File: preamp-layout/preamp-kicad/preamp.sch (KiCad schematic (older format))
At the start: 12 parts, among them P1 Conn_WallPlug, SW1 Rotary_Encoder_Switch, SW10 SW_Push_Open, SW11 SW_Push_Open, SW2 Rotary_Encoder_Switch, SW3 SW_SPST, SW4 SW_Push_Open, SW5 SW_Push_Open, SW6 SW_Push_Open, SW7 SW_Push_Open, SW8 SW_Push_Open, SW9 SW_Push_Open

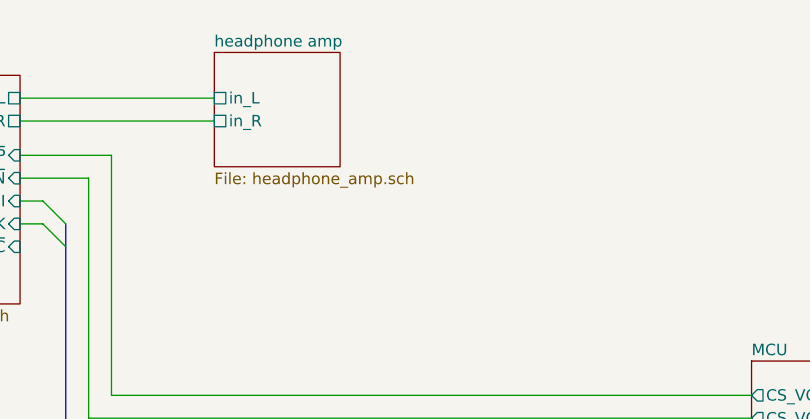
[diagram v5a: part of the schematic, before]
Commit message: Headphone Amp Crossfeed Implementation - using the CMOY modified Linkwitz High Z crossfeed design as a basis.
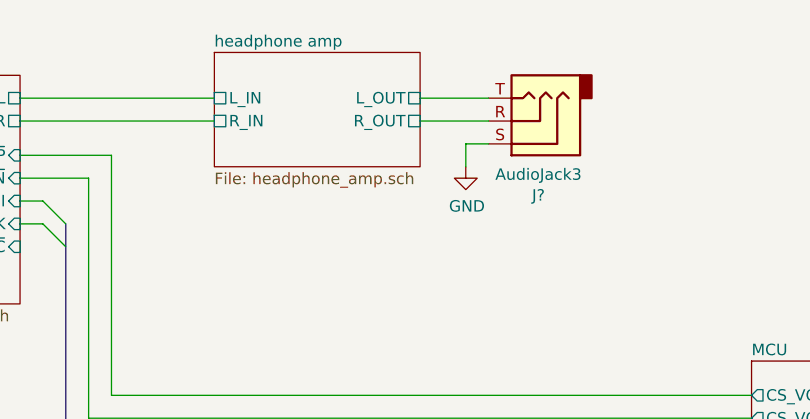
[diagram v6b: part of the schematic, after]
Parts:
- added J?: AudioJack3, symbol Connector:AudioJack3
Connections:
- net GND: now also J?.S
- new net headphone amp/L_OUT: J?.T
- new net headphone amp/R_OUT: J?.R
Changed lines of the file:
@@
 EESchema Schematic File Version 4
+LIBS:preamp-cache
 EELAYER 30 0
 EELAYER END
 $Descr A4 11693 8268
 encoding utf-8
-Sheet 1 12
+Sheet 1 13
 Title "Preamp"
-Date "2020-01-23"
+Date "2020-02-25"
 Rev "A00"
 Comp ""
@@
 F2 "AC+" U L 3200 7100 50
 F3 "AC-" U L 3200 7200 50
-$EndSheet
-$Sheet
-S 5850 950  550  500
-U 5E4A803E
-F0 "headphone amp" 50
-F1 "headphone_amp.sch" 50
-F2 "in_R" U L 5850 1250 50
-F3 "in_L" U L 5850 1150 50
 $EndSheet
 $Sheet
@@
 $EndSheet
 $Sheet
-S 1400 4350 550  550
-U 5E1A0CE1
-F0 "Balanced daughter IO pcb" 50
-F1 "IO_BALANCED_DAUGHTER.sch" 50
-F2 "OUT_R" U R 1950 4800 50
-F3 "OUT_L" U R 1950 4700 50
-F4 "IN_L" U R 1950 4450 50
-F5 "IN_R" U R 1950 4550 50
-$EndSheet
-$Sheet
 S 850  900  750  2450
 U 5E607732
@@
 F15 "A_OUT_2_L" U R 1600 3100 50
 $EndSheet
-Text Label 2200 4450 0    50   ~ 0
-BAL_IN_L
-Text Label 2200 4550 0    50   ~ 0
-BAL_IN_R
-Text Label 2200 4700 0    50   ~ 0
-BAL_OUT_L
-Text Label 2200 4800 0    50   ~ 0
-BAL_OUT_R
-Text Label 1950 2350 3    50   ~ 0
-BAL_IN_L
-Text Label 1850 2350 3    50   ~ 0
-BAL_IN_R
-Text Label 1950 3400 3    50   ~ 0
-BAL_OUT_L
-Text Label 1850 3400 3    50   ~ 0
-BAL_OUT_R
 $Comp
 L Device:Rotary_Encoder_Switch SW?
@@
 	2650 6150 3050 6150
 Wire Wire Line
-	1950 4450 2200 4450
-Wire Wire Line
-	1950 4550 2200 4550
-Wire Wire Line
-	1950 4700 2200 4700
-Wire Wire Line
-	1950 4800 2200 4800
-Wire Wire Line
 	1600 2850 2150 2850
 Wire Wire Line
 	1600 2950 2150 2950
 Wire Wire Line
-	1600 3100 1950 3100
-Wire Wire Line
-	1600 3200 1850 3200
-Wire Wire Line
-	1600 2150 1850 2150
-Wire Wire Line
-	1600 2050 1950 2050
-Wire Wire Line
 	1600 1000 2150 1000
 Wire Wire Line
@@
 Wire Wire Line
 	1600 1850 2150 1850
-Wire Wire Line
-	1950 2350 1950 2050
-Connection ~ 1950 2050
-Wire Wire Line
-	1950 2050 2150 2050
-Wire Wire Line
-	1850 2350 1850 2150
-Connection ~ 1850 2150
-Wire Wire Line
-	1850 2150 2150 2150
-Wire Wire Line
-	1950 3400 1950 3100
-Connection ~ 1950 3100
-Wire Wire Line
-	1950 3100 2150 3100
-Wire Wire Line
-	1850 3400 1850 3200
-Connection ~ 1850 3200
-Wire Wire Line
-	1850 3200 2150 3200
 Wire Wire Line
 	10450 2400 10750 2400
@@
 Connection ~ 10750 2900
 Connection ~ 10750 3450
-Wire Bus Line
-	5200 1700 5200 3300
-Wire Bus Line
-	8000 3300 8000 3500
-Wire Bus Line
-	3600 2850 3600 3300
-Wire Bus Line
-	6650 3300 6650 4050
 $Sheet
 S 4250 1050 750  1000
@@
 F12 "CLK" I R 5000 1700 50
 $EndSheet
+$Comp
+L Connector:AudioJack3 J?
+U 1 1 5F4B3F32
+P 7250 1250
+AR Path="/5E4A803E/5F4B3F32" Ref="J?"  Part="1"
+AR Path="/5F4B3F32" Ref="J?"  Part="1"
+F 0 "J?" H 7232 1575 50  0000 C CNN
+F 1 "AudioJack3" H 7232 1484 50  0000 C CNN
+F 2 "" H 7250 1250 50  0001 C CNN
+F 3 "~" H 7250 1250 50  0001 C CNN
+	1    7250 1250
+	-1   0    0    1
+$EndComp
+$Comp
+L power:GND #PWR?
+U 1 1 5F4B3F39
+P 6950 1450
+AR Path="/6009D432/5F4B3F39" Ref="#PWR?"  Part="1"
+AR Path="/5E4A803E/5F4B3F39" Ref="#PWR?"  Part="1"
+AR Path="/5F4B3F39" Ref="#PWR?"  Part="1"
+F 0 "#PWR?" H 6950 1200 50  0001 C CNN
+F 1 "GND" H 6955 1277 50  0000 C CNN
+F 2 "" H 6950 1450 50  0001 C CNN
+F 3 "" H 6950 1450 50  0001 C CNN
+	1    6950 1450
+	1    0    0    -1
+$EndComp
+Wire Wire Line
+	6950 1450 6950 1350
+Wire Wire Line
+	6950 1350 7050 1350
+Wire Wire Line
+	6750 1150 7050 1150
+Wire Wire Line
+	6750 1250 7050 1250
+$Sheet
+S 5850 950  900  500
+U 5E4A803E
+F0 "headphone amp" 50
+F1 "headphone_amp.sch" 50
+F2 "R_IN" U L 5850 1250 50
+F3 "L_IN" U L 5850 1150 50
+F4 "L_OUT" U R 6750 1150 50
+F5 "R_OUT" U R 6750 1250 50
+$EndSheet
+Wire Wire Line
+	1850 3200 2150 3200
+Wire Wire Line
+	1600 3200 1850 3200
+Connection ~ 1850 3200
+Wire Wire Line
+	1850 3400 1850 3200
+Wire Wire Line
+	1950 3100 2150 3100
+Wire Wire Line
+	1600 3100 1950 3100
+Connection ~ 1950 3100
+Wire Wire Line
+	1950 3400 1950 3100
+Text Label 1850 3400 3    50   ~ 0
+BAL_OUT_R
+Text Label 1950 3400 3    50   ~ 0
+BAL_OUT_L
+Wire Wire Line
+	1850 2150 2150 2150
+Wire Wire Line
+	1600 2150 1850 2150
+Connection ~ 1850 2150
+Wire Wire Line
+	1850 2350 1850 2150
+Wire Wire Line
+	1950 2050 2150 2050
+Wire Wire Line
+	1600 2050 1950 2050
+Connection ~ 1950 2050
+Wire Wire Line
+	1950 2350 1950 2050
+Text Label 1850 2350 3    50   ~ 0
+BAL_IN_R
+Text Label 1950 2350 3    50   ~ 0
+BAL_IN_L
+Wire Bus Line
+	5200 1700 5200 3300
+Wire Bus Line
+	6650 3300 6650 4050
+Wire Bus Line
+	8000 3300 8000 3500
+Wire Bus Line
+	3600 2850 3600 3300
+Wire Wire Line
+	1950 4800 2200 4800
+Wire Wire Line
+	1950 4700 2200 4700
+Wire Wire Line
+	1950 4550 2200 4550
+Wire Wire Line
+	1950 4450 2200 4450
+Text Label 2200 4800 0    50   ~ 0
+BAL_OUT_R
+Text Label 2200 4700 0    50   ~ 0
+BAL_OUT_L
+Text Label 2200 4550 0    50   ~ 0
+BAL_IN_R
+Text Label 2200 4450 0    50   ~ 0
+BAL_IN_L
+$Sheet
+S 1400 4350 550  550
+U 5E1A0CE1
+F0 "Balanced daughter IO pcb" 50
+F1 "IO_BALANCED_DAUGHTER.sch" 50
+F2 "OUT_R" U R 1950 4800 50
+F3 "OUT_L" U R 1950 4700 50
+F4 "IN_L" U R 1950 4450 50
+F5 "IN_R" U R 1950 4550 50
+$EndSheet
 $EndSCHEMATC

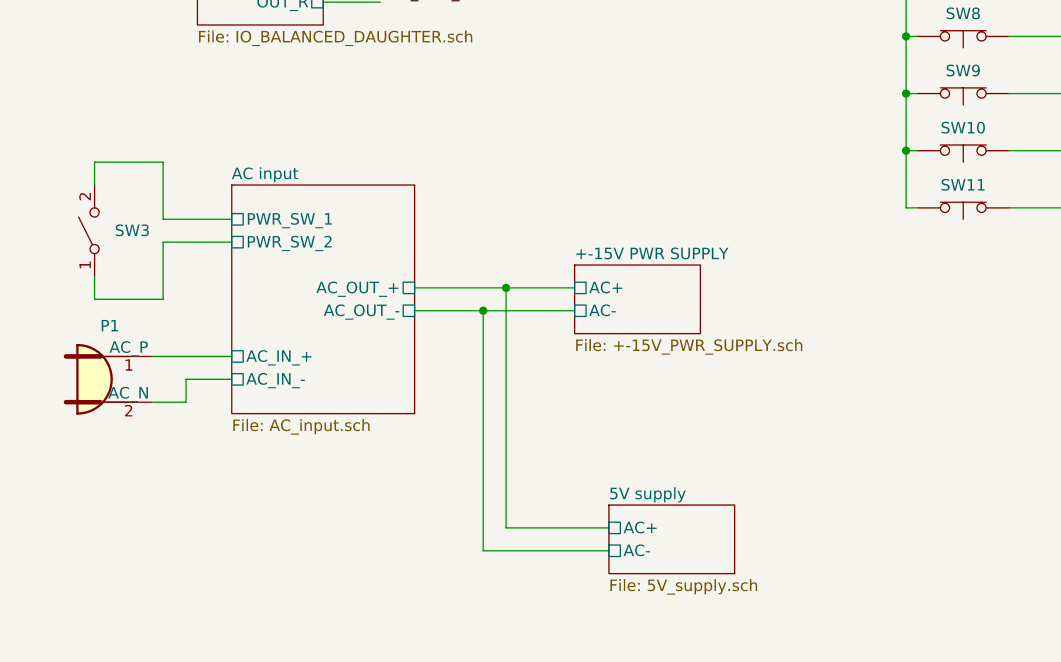
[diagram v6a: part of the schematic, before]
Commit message: Incorporated Standby Relay
The Relay shown on the AC Input page is meant to control the +/-15V supply. The coil is controlled by two pins on the esp32 MCU. The 5V supply will be active at all times. I think the working condition will be something like, both pins are low then one goes high to move the switch, then goes back to low. when another state change happens the other pin will go high and move the switch back, etc.
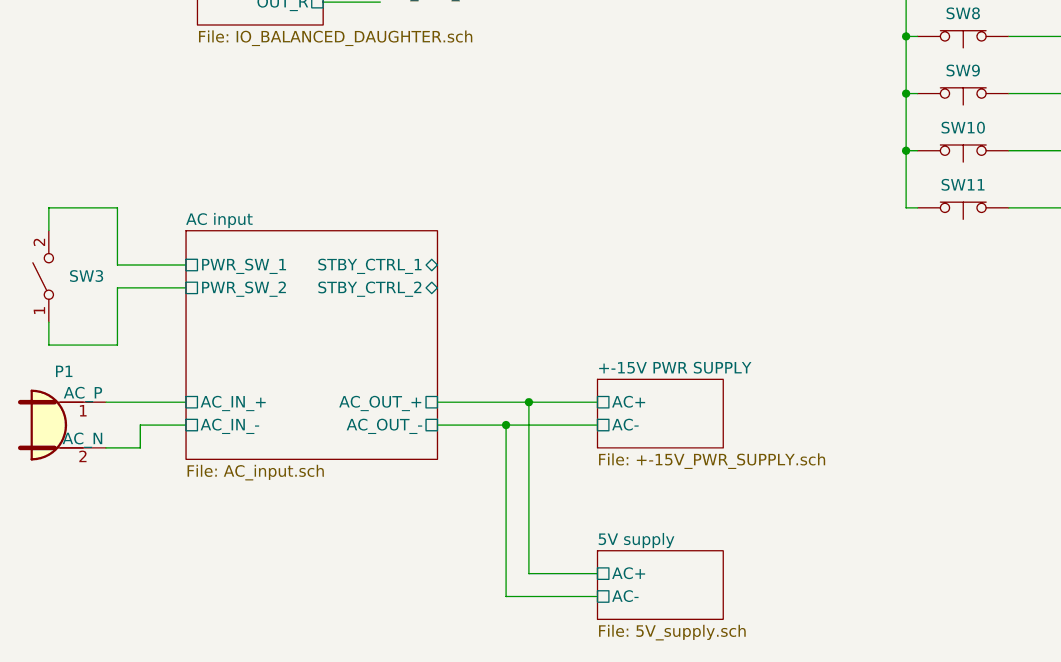
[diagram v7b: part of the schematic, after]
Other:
- moved on the sheet: P1, SW3
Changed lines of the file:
@@
 EESchema Schematic File Version 4
-LIBS:preamp-cache
 EELAYER 30 0
 EELAYER END
@@
 $EndDescr
 $Sheet
-S 1550 5600 800  1000
+S 1350 5800 1100 1000
 U 5E26F6FE
 F0 "AC input" 50
 F1 "AC_input.sch" 50
-F2 "PWR_SW_1" U L 1550 5750 50
-F3 "PWR_SW_2" U L 1550 5850 50
-F4 "AC_OUT_+" U R 2350 6050 50
-F5 "AC_IN_-" U L 1550 6450 50
-F6 "AC_IN_+" U L 1550 6350 50
-F7 "AC_OUT_-" U R 2350 6150 50
-$EndSheet
-$Sheet
-S 3050 5950 550  300
+F2 "PWR_SW_1" U L 1350 5950 50
+F3 "PWR_SW_2" U L 1350 6050 50
+F4 "AC_OUT_+" U R 2450 6550 50
+F5 "AC_IN_-" U L 1350 6650 50
+F6 "AC_IN_+" U L 1350 6550 50
+F7 "AC_OUT_-" U R 2450 6650 50
+F8 "STBY_CTRL_2" B R 2450 6050 50
+F9 "STBY_CTRL_1" B R 2450 5950 50
+$EndSheet
+$Sheet
+S 3150 6450 550  300
 U 5E27B612
 F0 "+-15V PWR SUPPLY" 50
 F1 "+-15V_PWR_SUPPLY.sch" 50
-F2 "AC+" U L 3050 6050 50
-F3 "AC-" U L 3050 6150 50
-$EndSheet
-$Sheet
-S 3200 7000 550  300
+F2 "AC+" U L 3150 6550 50
+F3 "AC-" U L 3150 6650 50
+$EndSheet
+$Sheet
+S 3150 7200 550  300
 U 5E5EF2D4
 F0 "5V supply" 50
 F1 "5V_supply.sch" 50
-F2 "AC+" U L 3200 7100 50
-F3 "AC-" U L 3200 7200 50
+F2 "AC+" U L 3150 7300 50
+F3 "AC-" U L 3150 7400 50
 $EndSheet
 $Sheet
@@
 	8000 3500 8100 3600
 Wire Wire Line
-	2350 6050 2750 6050
-Wire Wire Line
-	2350 6150 2650 6150
-Wire Wire Line
-	2750 6050 2750 7100
-Wire Wire Line
-	2750 7100 3200 7100
-Connection ~ 2750 6050
-Wire Wire Line
-	2750 6050 3050 6050
-Wire Wire Line
-	2650 6150 2650 7200
-Wire Wire Line
-	2650 7200 3200 7200
-Connection ~ 2650 6150
-Wire Wire Line
-	2650 6150 3050 6150
+	2450 6550 2850 6550
+Wire Wire Line
+	2450 6650 2750 6650
+Wire Wire Line
+	2850 6550 2850 7300
+Wire Wire Line
+	2850 6550 3150 6550
+Wire Wire Line
+	2750 6650 2750 7400
+Wire Wire Line
+	2750 6650 3150 6650
 Wire Wire Line
 	1600 2850 2150 2850
@@
 L Switch:SW_SPST SW?
 U 1 1 5E2E8D21
-P 950 5800
+P 750 6000
 AR Path="/5E26F6FE/5E2E8D21" Ref="SW?"  Part="1"
 AR Path="/5E2E8D21" Ref="SW3"  Part="1"
-F 0 "SW3" V 950 5712 50  0000 R CNN
-F 1 "SW_SPST" H 950 5944 50  0001 C CNN
-F 2 "" H 950 5800 50  0001 C CNN
-F 3 "~" H 950 5800 50  0001 C CNN
-	1    950  5800
+F 0 "SW3" V 750 5912 50  0000 R CNN
+F 1 "SW_SPST" H 750 6144 50  0001 C CNN
+F 2 "" H 750 6000 50  0001 C CNN
+F 3 "~" H 750 6000 50  0001 C CNN
+	1    750  6000
 	0    -1   -1   0
 $EndComp
 Wire Wire Line
-	950  5600 950  5500
-Wire Wire Line
-	950  5500 1250 5500
-Wire Wire Line
-	1250 5500 1250 5750
-Wire Wire Line
-	1250 5750 1550 5750
-Wire Wire Line
-	950  6000 950  6100
-Wire Wire Line
-	950  6100 1250 6100
-Wire Wire Line
-	1250 6100 1250 5850
-Wire Wire Line
-	1250 5850 1550 5850
+	750  5800 750  5700
+Wire Wire Line
+	750  5700 1050 5700
+Wire Wire Line
+	1050 5700 1050 5950
+Wire Wire Line
+	1050 5950 1350 5950
+Wire Wire Line
+	750  6200 750  6300
+Wire Wire Line
+	750  6300 1050 6300
+Wire Wire Line
+	1050 6300 1050 6050
+Wire Wire Line
+	1050 6050 1350 6050
 $Comp
 L Connector:Conn_WallPlug P?
 U 1 1 5E300B43
-P 1000 6450
+P 800 6650
 AR Path="/5E26F6FE/5E300B43" Ref="P?"  Part="1"
 AR Path="/5E300B43" Ref="P1"  Part="1"
-F 0 "P1" H 1017 6683 50  0000 C CNN
-F 1 "Conn_WallPlug" H 1017 6684 50  0001 C CNN
-F 2 "" H 1400 6450 50  0001 C CNN
-F 3 "~" H 1400 6450 50  0001 C CNN
-	1    1000 6450
+F 0 "P1" H 817 6883 50  0000 C CNN
+F 1 "Conn_WallPlug" H 817 6884 50  0001 C CNN
+F 2 "" H 1200 6650 50  0001 C CNN
+F 3 "~" H 1200 6650 50  0001 C CNN
+	1    800  6650
 	1    0    0    -1
 $EndComp
 Wire Wire Line
-	1200 6350 1550 6350
-Wire Wire Line
-	1200 6550 1350 6550
-Wire Wire Line
-	1350 6550 1350 6450
-Wire Wire Line
-	1350 6450 1550 6450
+	1000 6550 1350 6550
+Wire Wire Line
+	1000 6750 1150 6750
+Wire Wire Line
+	1150 6750 1150 6650
+Wire Wire Line
+	1150 6650 1350 6650
 $Sheet
 S 8250 4500 550  300
@@
 Text Label 1950 2350 3    50   ~ 0
 BAL_IN_L
-Wire Bus Line
-	5200 1700 5200 3300
-Wire Bus Line
-	6650 3300 6650 4050
-Wire Bus Line
-	8000 3300 8000 3500
-Wire Bus Line
-	3600 2850 3600 3300
 Wire Wire Line
 	1950 4800 2200 4800
@@
 F5 "IN_R" U R 1950 4550 50
 $EndSheet
+Connection ~ 2750 6650
+Connection ~ 2850 6550
+Wire Wire Line
+	3150 7300 2850 7300
+Wire Wire Line
+	3150 7400 2750 7400
+Wire Bus Line
+	5200 1700 5200 3300
+Wire Bus Line
+	8000 3300 8000 3500
+Wire Bus Line
+	3600 2850 3600 3300
+Wire Bus Line
+	6650 3300 6650 4050
 $EndSCHEMATC
